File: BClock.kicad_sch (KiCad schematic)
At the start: 2 parts, among them J1 Conn_01x03_Pin, J2 Conn_01x03_Pin

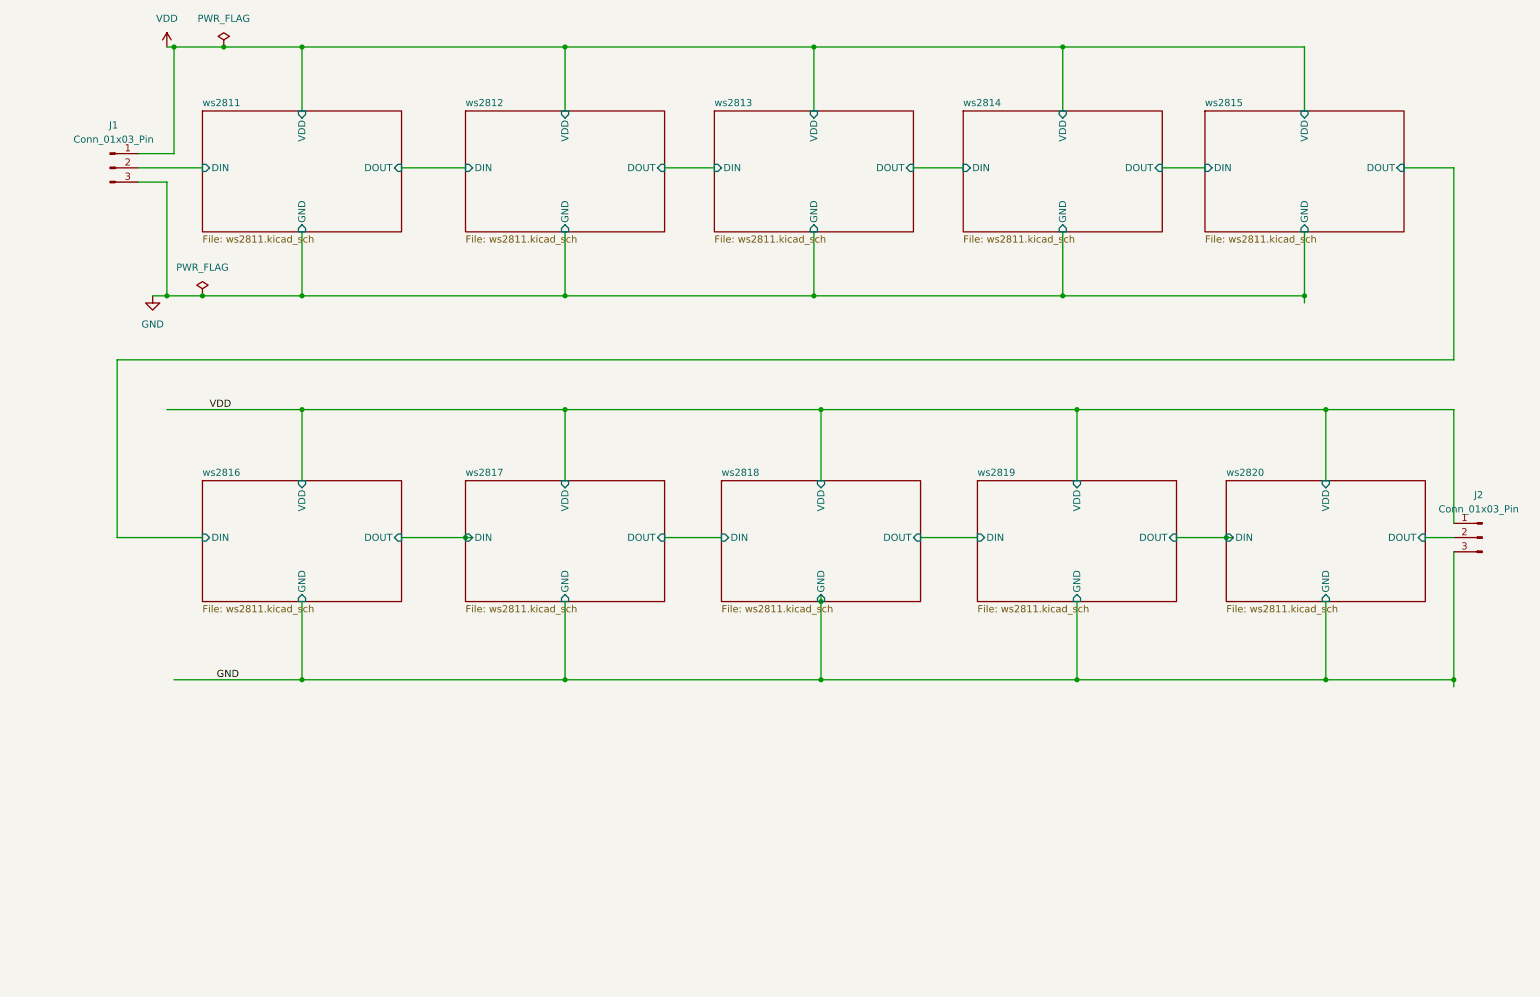
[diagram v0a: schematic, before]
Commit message: NEW: Added ESP32C3 and level shifter
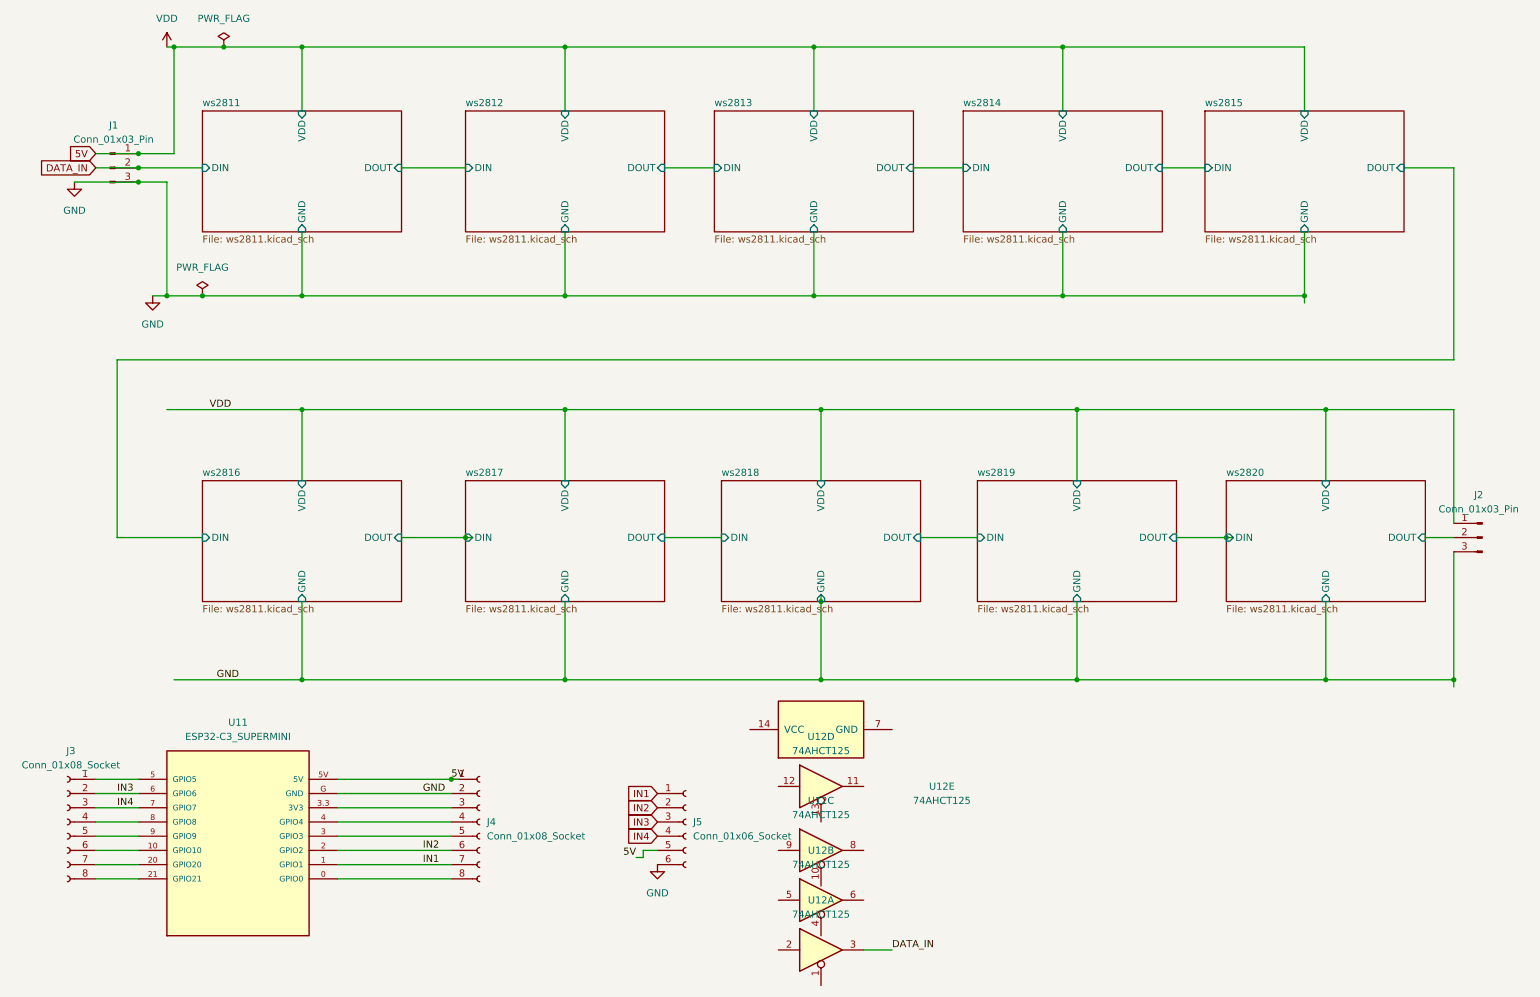
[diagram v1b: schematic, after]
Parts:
- added J3, J4: Conn_01x08_Socket, Connector_PinHeader_2.54mm:PinHeader_1x08_P2.54mm_Vertical, symbol Connector:Conn_01x08_Socket
- added J5: Conn_01x06_Socket, Connector_PinHeader_2.54mm:PinHeader_1x06_P2.54mm_Vertical, symbol Connector:Conn_01x06_Socket
- added U11: ESP32-C3_SUPERMINI, Mikes Library:MODULE_ESP32-C3_SUPERMINI, symbol Mikes Library:ESP32-C3_SUPERMINI
- added U12: 74AHCT125, Package_DIP:DIP-14_W10.16mm, symbol 74xx:74AHCT125
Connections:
- net GND: now also J4.2 (Pin_2), J5.6 (Pin_6), U11.G (GND)
- net VDD: now also J4.1 (Pin_1), J5.5 (Pin_5), U11.5V
- net ws2811/DIN renamed DATA_IN
- net DATA_IN: now also U12.3
- new net: J4.3 (Pin_3), U11.3.3 (3V3)
- new net: J4.4 (Pin_4), U11.4 (GPIO4)
- new net: J4.5 (Pin_5), U11.3 (GPIO3)
- new net: J4.8 (Pin_8), U11.0 (GPIO0)
- new net: J3.6 (Pin_6), U11.10 (GPIO10)
- new net: J3.7 (Pin_7), U11.20 (GPIO20)
- new net: J3.8 (Pin_8), U11.21 (GPIO21)
- new net: J3.1 (Pin_1), U11.5 (GPIO5)
- new net: J3.4 (Pin_4), U11.8 (GPIO8)
- new net: J3.5 (Pin_5), U11.9 (GPIO9)
- new net IN1: J4.7 (Pin_7), J5.1 (Pin_1), U11.1 (GPIO1)
- new net IN2: J4.6 (Pin_6), J5.2 (Pin_2), U11.2 (GPIO2)
- new net IN3: J3.2 (Pin_2), J5.3 (Pin_3), U11.6 (GPIO6)
- new net IN4: J3.3 (Pin_3), J5.4 (Pin_4), U11.7 (GPIO7)
